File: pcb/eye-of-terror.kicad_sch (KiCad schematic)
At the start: 217 parts, among them J1 Conn_01x02_Socket, J10 Conn_01x03, J11 Conn_01x03, J12 Conn_01x03, J13 Conn_01x03, J14 Conn_01x03, J15 Conn_01x03, J16 Conn_01x03, J2 G-Switch GT-USB-7055E, J3 Conn_01x04, J4 Conn_01x04, J5 Conn_01x03, J6 Conn_01x02_Socket, J7 Conn_01x02_Socket, J8 Conn_01x03, J9 Conn_01x03, Q1 IPT020N10N3, Q2 IPT020N10N3, Q3 IPT020N10N3, Q4 IPT020N10N3, Q5 IPT020N10N3, Q6 IPT020N10N3, SW1 SW_Push, SW2 SW_Push, U1 RP2350B, U2 TD1660, U3 AP63205WU-7, U4 LSM6DS3, U5 W25Q32JVSS, U7 DRV8353HRTAR, Y1 ABM8-272-T3

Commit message: updated smaller footprints for some components
added lock files to gitignore
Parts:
- C10, C11, C14, C15, C16, C17, C18, C19, C20, C21, C22, C23, C24, C25, C26, C27, C28, C29, C8: footprint Capacitor_SMD:C_0603_1608Metric -> Capacitor_SMD:C_0402_1005Metric
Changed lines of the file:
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@@
 			)
 		)
-		(property "Footprint" "Capacitor_SMD:C_0603_1608Metric"
+		(property "Footprint" "Capacitor_SMD:C_0402_1005Metric"
 			(at 27.94 344.17 0)
 			(effects
@@
 			)
 		)
-		(property "Footprint" "Capacitor_SMD:C_0603_1608Metric"
+		(property "Footprint" "Capacitor_SMD:C_0402_1005Metric"
 			(at 111.76 31.75 0)
 			(effects
@@
 			)
 		)
-		(property "Footprint" "Capacitor_SMD:C_0603_1608Metric"
+		(property "Footprint" "Capacitor_SMD:C_0402_1005Metric"
 			(at 123.19 31.75 0)
 			(effects
@@
 			)
 		)
-		(property "Footprint" "Capacitor_SMD:C_0603_1608Metric"
+		(property "Footprint" "Capacitor_SMD:C_0402_1005Metric"
 			(at 82.55 34.29 0)
 			(effects
@@
 			)
 		)
-		(property "Footprint" "Capacitor_SMD:C_0603_1608Metric"
+		(property "Footprint" "Capacitor_SMD:C_0402_1005Metric"
 			(at 161.29 72.39 0)
 			(effects
@@
 			)
 		)
-		(property "Footprint" "Capacitor_SMD:C_0603_1608Metric"
+		(property "Footprint" "Capacitor_SMD:C_0402_1005Metric"
 			(at 99.06 31.75 0)
 			(effects
@@
 			)
 		)
-		(property "Footprint" "Capacitor_SMD:C_0603_1608Metric"
+		(property "Footprint" "Capacitor_SMD:C_0402_1005Metric"
 			(at 147.32 52.07 0)
 			(effects
@@
 			)
 		)
-		(property "Footprint" "Capacitor_SMD:C_0603_1608Metric"
+		(property "Footprint" "Capacitor_SMD:C_0402_1005Metric"
 			(at 193.04 220.98 0)
 			(effects
@@
 			)
 		)
-		(property "Footprint" "Capacitor_SMD:C_0603_1608Metric"
+		(property "Footprint" "Capacitor_SMD:C_0402_1005Metric"
 			(at 76.2 212.09 0)
 			(effects
@@
 			)
 		)
-		(property "Footprint" "Capacitor_SMD:C_0603_1608Metric"
+		(property "Footprint" "Capacitor_SMD:C_0402_1005Metric"
 			(at 62.23 34.29 0)
 			(effects
@@
 			)
 		)
-		(property "Footprint" "Capacitor_SMD:C_0603_1608Metric"
+		(property "Footprint" "Capacitor_SMD:C_0402_1005Metric"
 			(at 77.47 34.29 0)
 			(effects
@@
 			)
 		)
-		(property "Footprint" "Capacitor_SMD:C_0603_1608Metric"
+		(property "Footprint" "Capacitor_SMD:C_0402_1005Metric"
 			(at 57.15 34.29 0)
 			(effects
@@
 			)
 		)
-		(property "Footprint" "Capacitor_SMD:C_0603_1608Metric"
+		(property "Footprint" "Capacitor_SMD:C_0402_1005Metric"
 			(at 41.91 34.29 0)
 			(effects
@@
 			)
 		)
-		(property "Footprint" "Capacitor_SMD:C_0603_1608Metric"
+		(property "Footprint" "Capacitor_SMD:C_0402_1005Metric"
 			(at 67.31 34.29 0)
 			(effects
@@
 			)
 		)
-		(property "Footprint" "Capacitor_SMD:C_0603_1608Metric"
+		(property "Footprint" "Capacitor_SMD:C_0402_1005Metric"
 			(at 52.07 34.29 0)
 			(effects
@@
 			)
 		)
-		(property "Footprint" "Capacitor_SMD:C_0603_1608Metric"
+		(property "Footprint" "Capacitor_SMD:C_0402_1005Metric"
 			(at 144.78 27.94 0)
 			(effects
@@
 			)
 		)
-		(property "Footprint" "Capacitor_SMD:C_0603_1608Metric"
+		(property "Footprint" "Capacitor_SMD:C_0402_1005Metric"
 			(at 72.39 34.29 0)
 			(effects
@@
 			)
 		)
-		(property "Footprint" "Capacitor_SMD:C_0603_1608Metric"
+		(property "Footprint" "Capacitor_SMD:C_0402_1005Metric"
 			(at 46.99 34.29 0)
 			(effects
@@
 			)
 		)
-		(property "Footprint" "Capacitor_SMD:C_0603_1608Metric"
+		(property "Footprint" "Capacitor_SMD:C_0402_1005Metric"
 			(at 33.02 212.09 0)
 			(effects

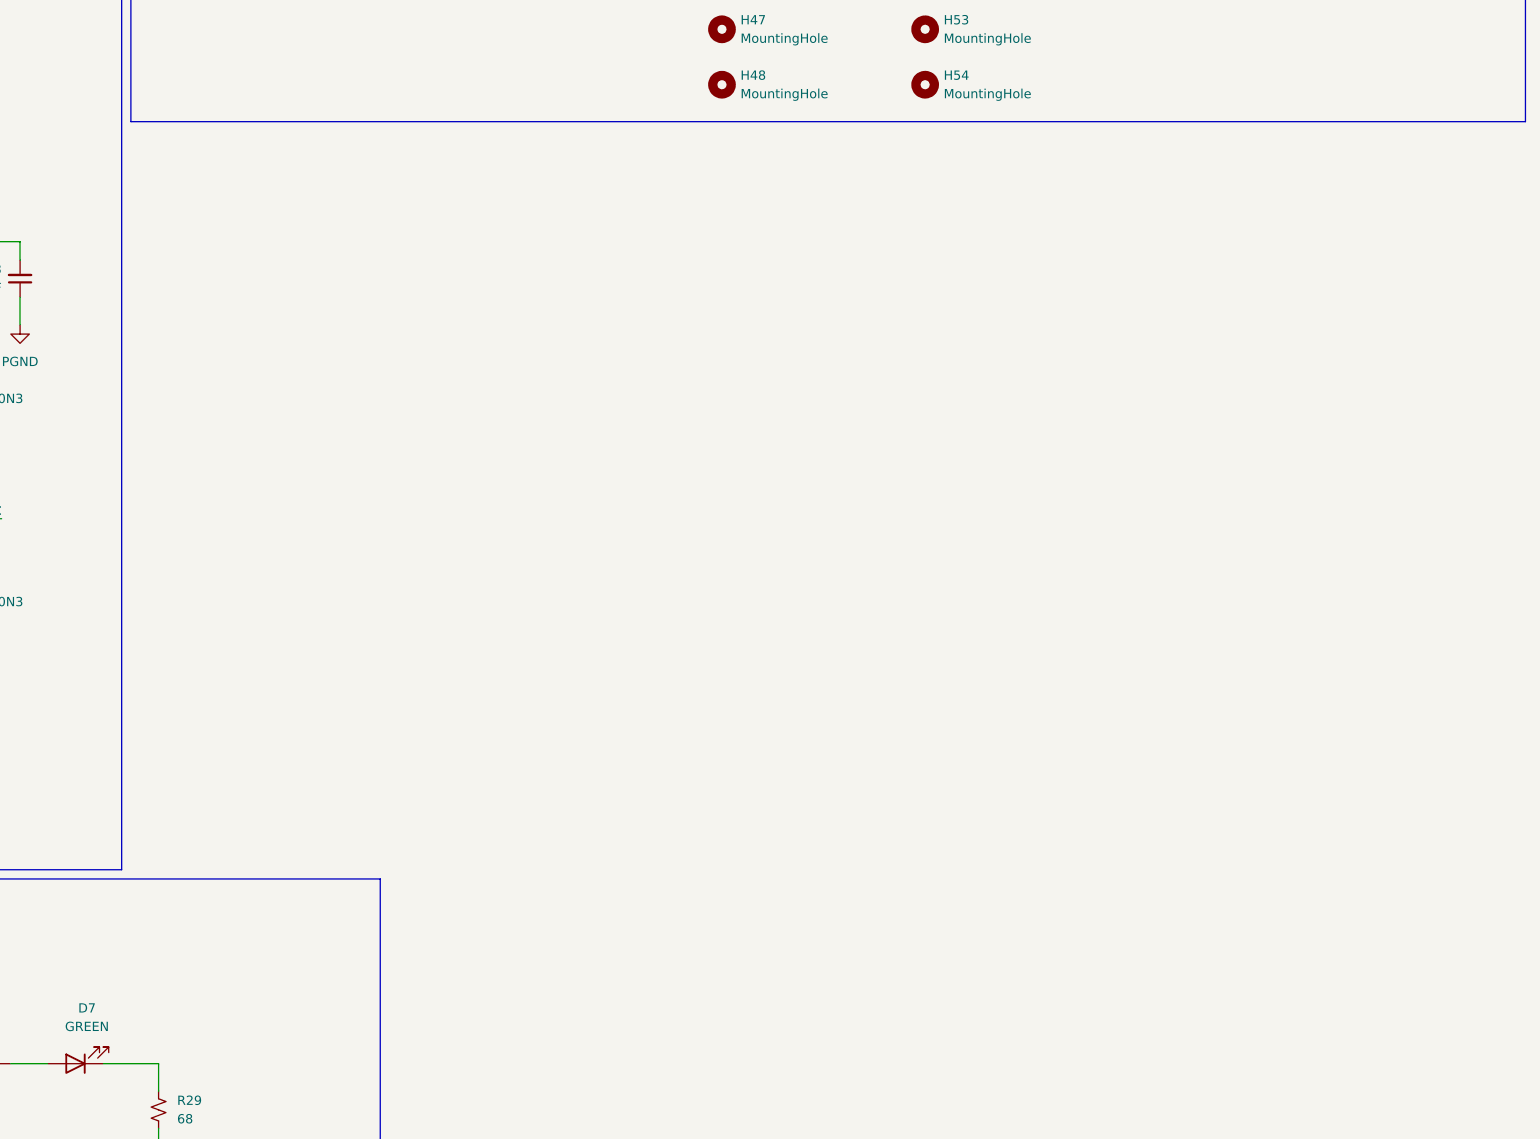
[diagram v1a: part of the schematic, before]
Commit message: added encoder diodes and phototransistors back in
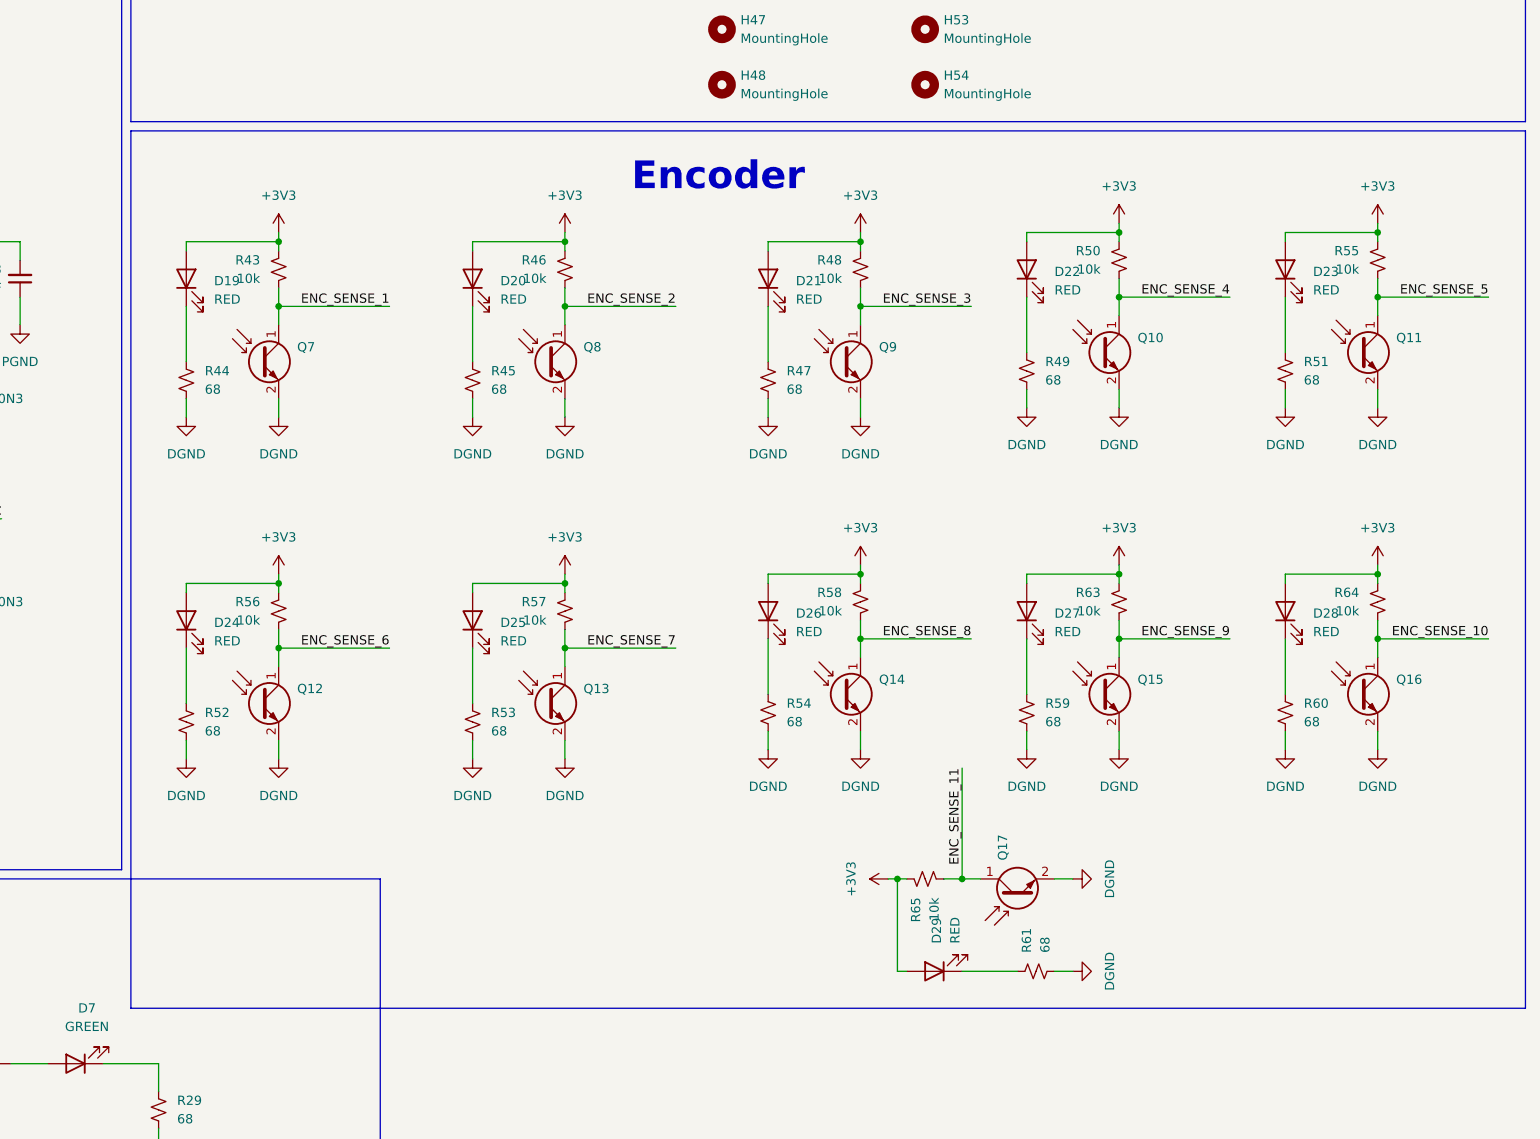
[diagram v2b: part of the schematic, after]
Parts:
- added D19, D20, D21, D22, D23, D24, D25, D26, D27, D28, D29: RED, Diode_SMD:D_1206_3216Metric, symbol Device:LED
- added Q10, Q11, Q12, Q13, Q14, Q15, Q16, Q17, Q7, Q8, Q9: ALS-PT19-315C/L177/TR8, LED_SMD:LED_0603_1608Metric, symbol Device:Q_Photo_NPN
- added R43, R46, R48, R50, R55, R56, R57, R58, R63, R64, R65: 10k, Resistor_SMD:R_0402_1005Metric, symbol Device:R_Small_US
- added R44, R45, R47, R49, R51, R52, R53, R54, R59, R60, R61: 68, Resistor_SMD:R_0402_1005Metric, symbol Device:R_Small_US
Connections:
- net +3V3: now also D19.2 (A), D20.2 (A), D21.2 (A), D22.2 (A), D23.2 (A), D24.2 (A), D25.2 (A), D26.2 (A), D27.2 (A), D28.2 (A), D29.2 (A), R43.1, R46.1, R48.1, R50.1, R55.1, R56.1, R57.1, R58.1, R63.1, R64.1, R65.1
- net DGND: now also Q10.2 (E), Q11.2 (E), Q12.2 (E), Q13.2 (E), Q14.2 (E), Q15.2 (E), Q16.2 (E), Q17.2 (E), Q7.2 (E), Q8.2 (E), Q9.2 (E), R44.2, R45.2, R47.2, R49.2, R51.2, R52.2, R53.2, R54.2, R59.2, R60.2, R61.2
- new net: D28.1 (K), R60.1
- new net: D20.1 (K), R45.1
- new net: D22.1 (K), R49.1
- new net: D23.1 (K), R51.1
- new net: D24.1 (K), R52.1
- new net: D19.1 (K), R44.1
- new net: D21.1 (K), R47.1
- new net: D25.1 (K), R53.1
- new net: D29.1 (K), R61.1
- new net: D27.1 (K), R59.1
- new net: D26.1 (K), R54.1
- new net ENC_SENSE_1: Q7.1 (C), R43.2
- new net ENC_SENSE_10: Q16.1 (C), R64.2
- new net ENC_SENSE_11: Q17.1 (C), R65.2
- new net ENC_SENSE_2: Q8.1 (C), R46.2
- new net ENC_SENSE_3: Q9.1 (C), R48.2
- new net ENC_SENSE_4: Q10.1 (C), R50.2
- new net ENC_SENSE_5: Q11.1 (C), R55.2
- new net ENC_SENSE_6: Q12.1 (C), R56.2
- new net ENC_SENSE_7: Q13.1 (C), R57.2
- new net ENC_SENSE_8: Q14.1 (C), R58.2
- new net ENC_SENSE_9: Q15.1 (C), R63.2
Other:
- note added: "Encoder"

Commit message: added power and ground planes to middle layers
* removed net ties (for now)
* removed extra gpio pin nets
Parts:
- removed D10, D11, D9: RED, Diode_SMD:D_1206_3216Metric, symbol Device:LED
- removed J10, J11, J12, J13, J14, J15, J16, J8, J9: Conn_01x03, Connector_PinHeader_2.54mm:PinHeader_1x03_P2.54mm_Vertical, symbol Connector_Generic:Conn_01x03
- removed JP17, JP18, JP19, JP20, JP21, JP22, JP23, JP24, JP25: SolderJumper_3_Open, Jumper:SolderJumper-3_P1.3mm_Open_RoundedPad1.0x1.5mm, symbol Jumper:SolderJumper_3_Open
- removed NT2, NT3, NT4, NT5, NT6: NetTie_2, NetTie:NetTie-2_SMD_Pad2.0mm, symbol Device:NetTie_2
- removed R31, R32, R33: 68, Resistor_SMD:R_0402_1005Metric, symbol Device:R_Small_US
- D18: value RED -> GREEN
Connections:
- net DGND: now also R21.2, R23.2
- net PGND: no longer R21.2, R23.2
- net GPIO1: no longer names the net of U1.78 (GPIO1)
- net GPIO2: no longer names the net of U1.79 (GPIO2)
- net GPIO24: no longer names the net of U1.25 (GPIO24)
- net GPIO3: no longer names the net of U1.80 (GPIO3)
- net GPIO36: no longer names the net of U1.45 (GPIO36)
- net GPIO37: no longer names the net of U1.46 (GPIO37)
- net GPIO38: no longer names the net of U1.47 (GPIO38)
- net GPIO39: no longer names the net of U1.48 (GPIO39)
- net RED_LED_0: no longer names the net of U1.26 (GPIO25)
- net RED_LED_1: no longer names the net of U1.27 (GPIO26)
- net RED_LED_2: no longer names the net of U1.28 (GPIO27)
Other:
- moved on the sheet: R20, R21, R22, R23

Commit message: assigned pins to encoder phototransistors
* re-routed some motor driver pins and other stuff
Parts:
- removed D12, D14: GREEN, Diode_SMD:D_1206_3216Metric, symbol Device:LED
- removed D15, D17: BLUE, Diode_SMD:D_1206_3216Metric, symbol Device:LED
- removed R34, R36: 68, Resistor_SMD:R_0402_1005Metric, symbol Device:R_Small_US
- removed R37, R39: 15, Resistor_SMD:R_0603_1608Metric, symbol Device:R_Small_US
- added J8: Conn_01x03, Connector_PinHeader_2.54mm:PinHeader_1x03_P2.54mm_Vertical, symbol Connector_Generic:Conn_01x03
- added JP8: SolderJumper_3_Open, symbol Jumper:SolderJumper_3_Open
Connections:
- net BLUE_LED_0 is gone; now on net ENC_SENSE_4: U1.39 (GPIO31)
- net BLUE_LED_2 is gone; now on net ENC_SENSE_6: U1.42 (GPIO33)
- net GREEN_LED_0 is gone; now on net ENC_SENSE_1: U1.36 (GPIO28)
- net GREEN_LED_2 is gone; now on net ENC_SENSE_3: U1.38 (GPIO30)
- net +3V3: now also JP8.3 (B)
- net +5V: now also JP8.1 (A)
- net BLUE_LED_1: now also U1.79 (GPIO2); no longer U1.40 (GPIO32)
- net DGND: now also J8.3 (Pin_3)
- net DRIVER_ENABLE: now also U1.25 (GPIO24); no longer U1.43 (GPIO34)
- net DRIVER_FAULTn: now also U1.26 (GPIO25); no longer U1.44 (GPIO35)
- net ENC_SENSE_10: now also U1.46 (GPIO37)
- net ENC_SENSE_11: now also U1.47 (GPIO38)
- net ENC_SENSE_2: now also U1.37 (GPIO29)
- net ENC_SENSE_5: now also U1.40 (GPIO32)
- net ENC_SENSE_7: now also U1.43 (GPIO34)
- net ENC_SENSE_8: now also U1.44 (GPIO35)
- net ENC_SENSE_9: now also U1.45 (GPIO36)
- net GREEN_LED_1: now also U1.78 (GPIO1); no longer U1.37 (GPIO29)
- net GPIO3: now reaches U1.80 (GPIO3)
- net GPIO3: now also J8.2 (Pin_2)
- new net: J8.1 (Pin_1), JP8.2 (C)
- no-connect marks 5 -> 8
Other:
- note added: "Extra GPIO Pin"
- note removed: "Extra GPIO Breakout Pins"
- moved on the sheet: D13, D16, D19, D20, D21, D22, D23, D24, D25, D26, D27, D28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

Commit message: routed GPIO and debug LEDs
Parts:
- JP8: footprint (none) -> Jumper:SolderJumper-3_P1.3mm_Open_RoundedPad1.0x1.5mm_NumberLabels
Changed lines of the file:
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@@
 			)
 		)
-		(property "Footprint" ""
+		(property "Footprint" "Jumper:SolderJumper-3_P1.3mm_Open_RoundedPad1.0x1.5mm_NumberLabels"
 			(at 187.96 95.25 0)
 			(effects
